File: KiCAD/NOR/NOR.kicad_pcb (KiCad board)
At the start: 2 copper layers, 58.4 x 52.1 mm, 13 parts, among them J1 Conn_01x02_Pin, J2 Conn_01x02_Pin, J3 Conn_01x02_Pin, J4 Conn_01x02_Pin, Q13 2N7000, Q14 2N7000, Q3 2N7000, Q4 2N7000, Y1 Conn_01x01_Pin

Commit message: Cleanup
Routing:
- net (no net): track 32.9 -> 36.9 mm
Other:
- board text added: "All schematics, designs, and documentation for this project are released under the most permissive licence I could find:"
- board text added: "Copyright BlueChip 2025. This source describes Open Hardware and is licensed under the CERN-OHL-P v2 You may redistribute and modify this documentation and make products using it under the terms of the CERN-OHL-P v2 (https:/cern.ch/cern-ohl). This documentation is distributed WITHOUT ANY EXPRESS OR IMPLIED WARRANTY, INCLUDING OF MERCHANTABILITY, SATISFACTORY QUALITY AND FITNESS FOR A PARTICULAR P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"
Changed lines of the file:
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@@
+		(layer "B.SilkS")
+	)
+	(gr_rect
+		(start 205.718702 112.8075)
+		(end 227.943702 124.8725)
+		(stroke
+			(width 0.127)
+			(type dot)
+		)
+		(fill no)
 		(layer "B.SilkS")
 	)
@@
 		)
 	)
+	(gr_text "All schematics, designs, and\ndocumentation for this project\nare released under the most\npermissive licence I could find:"
+		(at 218.736202 111.22 0)
+		(layer "B.SilkS")
+		(effects
+			(font
+				(size 0.508 0.508)
+				(thickness 0.0635)
+			)
+			(justify bottom mirror)
+		)
+	)
 	(gr_text "D"
 		(at 230.166202 124.555 0)
@@
 				(thickness 0.2032)
 				(bold yes)
+			)
+			(justify left bottom mirror)
+		)
+	)
+	(gr_text "Copyright BlueChip 2025.\n\nThis source describes Open Hardware and is licensed \nunder the CERN-OHL-P v2\n\nYou may redistribute and modify this documentation \nand make products using it under the terms of the \nCERN-OHL-P v2 (https:/cern.ch/cern-ohl).\n\nThis documentation is distributed WITHOUT ANY EXPRESS \nOR IMPLIED WARRANTY, INCLUDING OF MERCHANTABILITY, \nSATISFACTORY QUALITY AND FITNESS FOR A PARTICULAR \nPURPOSE. \n\nPlease see the CERN-OHL-P v2 for applicable conditions."
+		(at 227.141426 124.238167 0)
+		(layer "B.SilkS")
+		(effects
+			(font
+				(size 0.4572 0.4572)
+				(thickness 0.05715)
 			)
 			(justify left bottom mirror)
@@
 	)
 	(segment
+		(start 237.913202 111.728)
+		(end 238.929202 111.728)
+		(width 0.2)
+		(layer "F.Cu")
+		(net 0)
+	)
+	(segment
+		(start 238.421202 112.236)
+		(end 238.421202 113.252)
+		(width 0.2)
+		(layer "F.Cu")
+		(net 0)
+	)
+	(segment
 		(start 213.529202 105.505)
 		(end 210.608202 105.505)
@@
 	)
 	(segment
+		(start 237.913202 111.728)
+		(end 238.929202 111.728)
+		(width 0.2)
+		(layer "B.Cu")
+		(net 0)
+	)
+	(segment
 		(start 213.021202 104.87)
 		(end 213.021202 102.093079)
@@
 		(layer "B.Cu")
 		(net 0)
+	)
+	(segment
+		(start 238.421202 112.236)
+		(end 238.421202 113.252)
+		(width 0.2)
+		(layer "B.Cu")
+		(net 0)

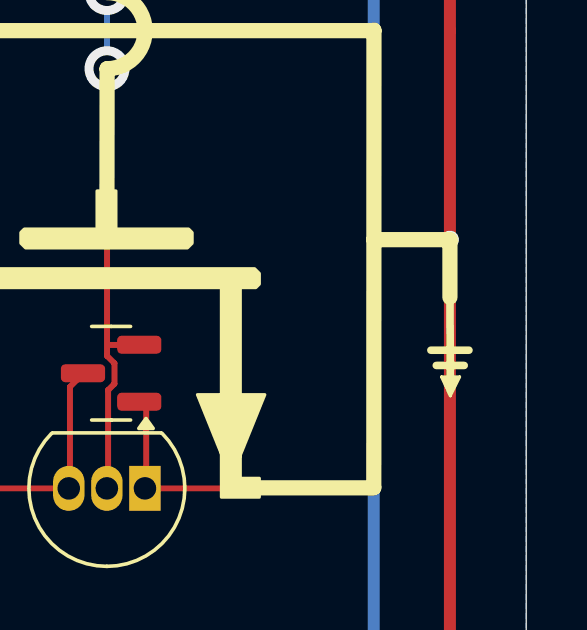
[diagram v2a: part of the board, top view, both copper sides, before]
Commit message: KiCAD: (N)AND_LED
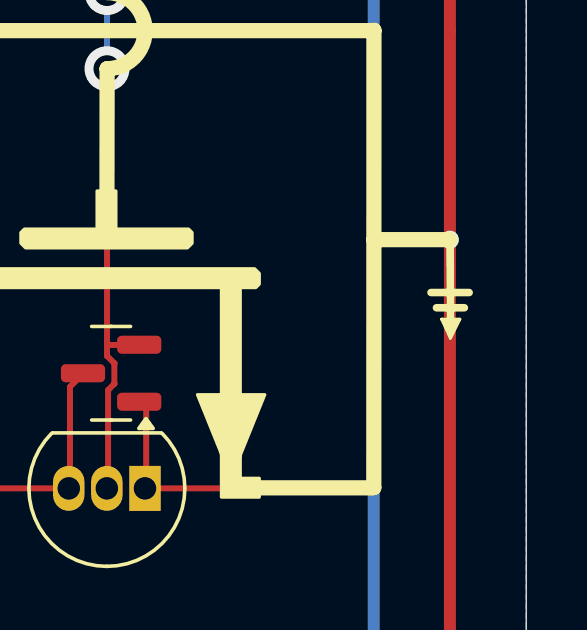
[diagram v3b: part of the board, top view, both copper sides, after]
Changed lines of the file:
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@@
 	)
 	(gr_line
-		(start 257.490157 138.41351)
-		(end 257.471202 135.35)
+		(start 257.495605 136.490537)
+		(end 257.47665 133.427027)
 		(stroke
 			(width 0.254)
@@
 	)
 	(gr_line
-		(start 256.836202 137.11249)
-		(end 258.106202 137.11249)
+		(start 256.84165 135.189517)
+		(end 258.11165 135.189517)
 		(stroke
 			(width 0.254)
@@
 	)
 	(gr_line
-		(start 257.308455 138.102543)
-		(end 257.655503 138.102543)
+		(start 257.313903 136.17957)
+		(end 257.660951 136.17957)
 		(stroke
 			(width 0.2032)
@@
 	)
 	(gr_line
-		(start 257.482858 138.63649)
-		(end 257.190949 138.00149)
+		(start 257.488306 136.713517)
+		(end 257.196397 136.078517)
 		(stroke
 			(width 0.1)
@@
 	)
 	(gr_line
-		(start 257.016476 137.62049)
-		(end 257.947822 137.62049)
+		(start 257.021924 135.697517)
+		(end 257.95327 135.697517)
 		(stroke
 			(width 0.254)
@@
 	)
 	(gr_line
-		(start 257.190949 138.00149)
-		(end 257.79666 138.00149)
+		(start 257.196397 136.078517)
+		(end 257.802108 136.078517)
 		(stroke
 			(width 0.1)
@@
 	)
 	(gr_line
-		(start 257.471202 135.35)
-		(end 257.471202 133.445)
-		(stroke
-			(width 0.508)
-			(type default)
-		)
-		(layer "F.SilkS")
-	)
-	(gr_line
 		(start 208.408801 149.581974)
 		(end 209.678801 149.581974)
@@
 	)
 	(gr_line
-		(start 257.374405 138.210656)
-		(end 257.598202 138.207412)
+		(start 257.379853 136.287683)
+		(end 257.60365 136.284439)
 		(stroke
 			(width 0.1)
@@
 	)
 	(gr_line
-		(start 257.79666 138.00149)
-		(end 257.482858 138.63649)
-		(stroke
-			(width 0.1)
+		(start 257.802108 136.078517)
+		(end 257.488306 136.713517)
+		(stroke
+			(width 0.1)
